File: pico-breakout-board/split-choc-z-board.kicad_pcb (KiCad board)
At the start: 2 copper layers, 147.1 x 106.5 mm, 79 parts, among them J1 USB4105-GF-A, J2 USB4105-GF-A, J3 Conn_01x04_Pin, J4 Conn_01x02, SW1 SW_SPST, SW10 SW_SPST, SW11 SW_SPST, SW12 SW_SPST, SW13 SW_SPST, SW14 SW_SPST, SW15 SW_SPST, SW16 SW_SPST, SW17 SW_SPST, SW18 SW_SPST, SW19 SW_SPST, SW2 SW_SPST, SW20 SW_SPST, SW21 SW_SPST, SW22 SW_SPST, SW3 SW_SPST, SW4 SW_SPST, SW5 SW_SPST, SW6 SW_SPST, SW7 SW_SPST, SW8 SW_SPST, SW9 SW_SPST, U2 RP2040, U3 NCP1117-3.3_SOT223, U4 W25Q128JVS, U5 USBLC6-2SC6, X1 ABM8-272-T3

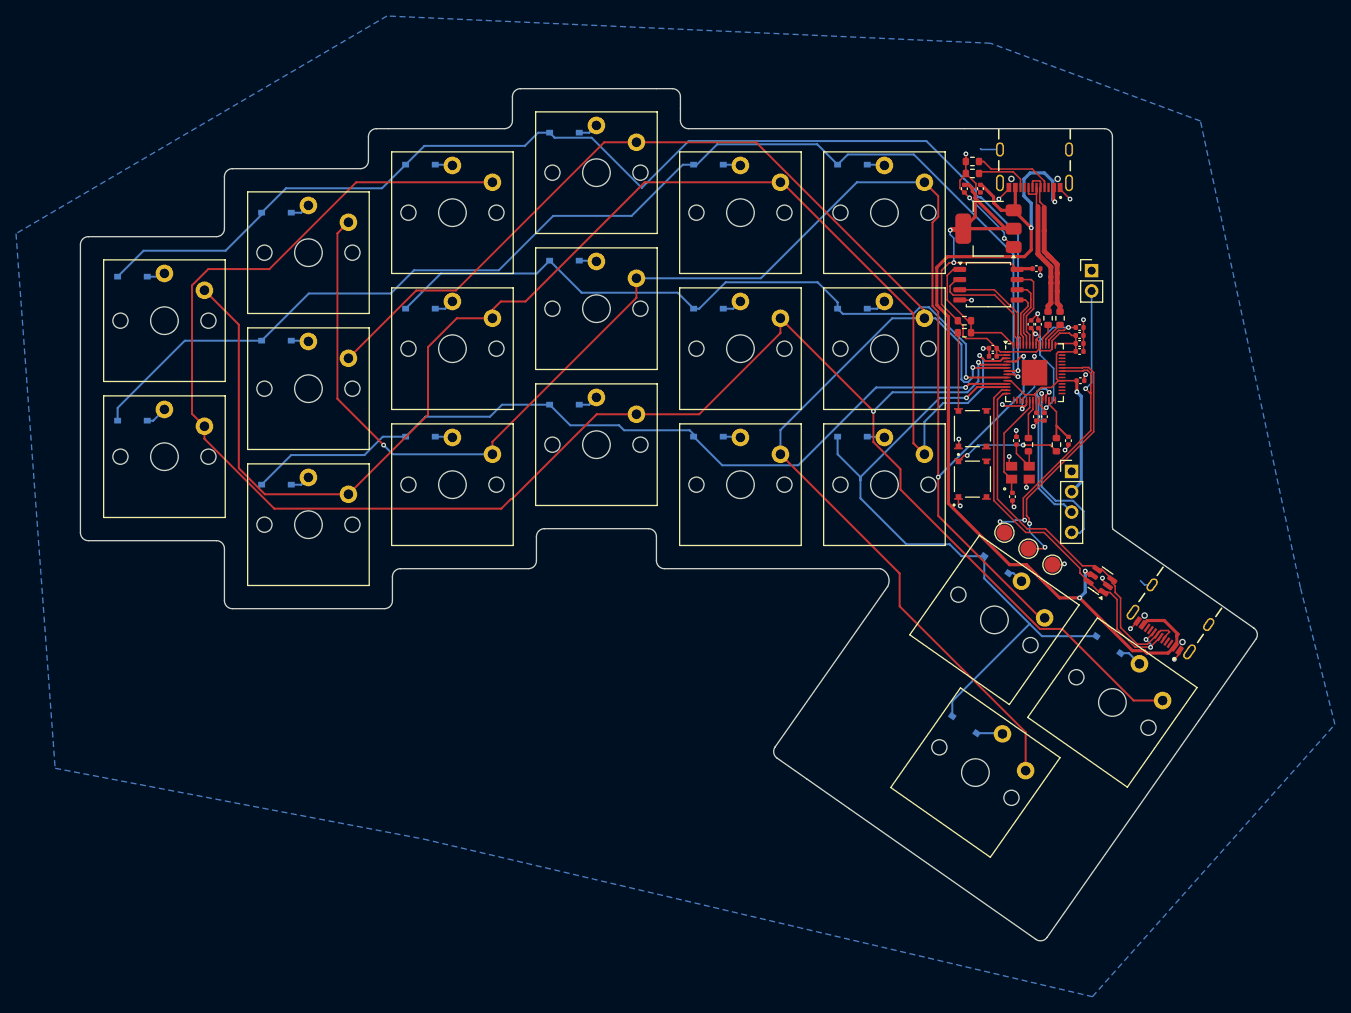
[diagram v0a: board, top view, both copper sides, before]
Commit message: Removed matrix and added 2.54mm pins 2x20
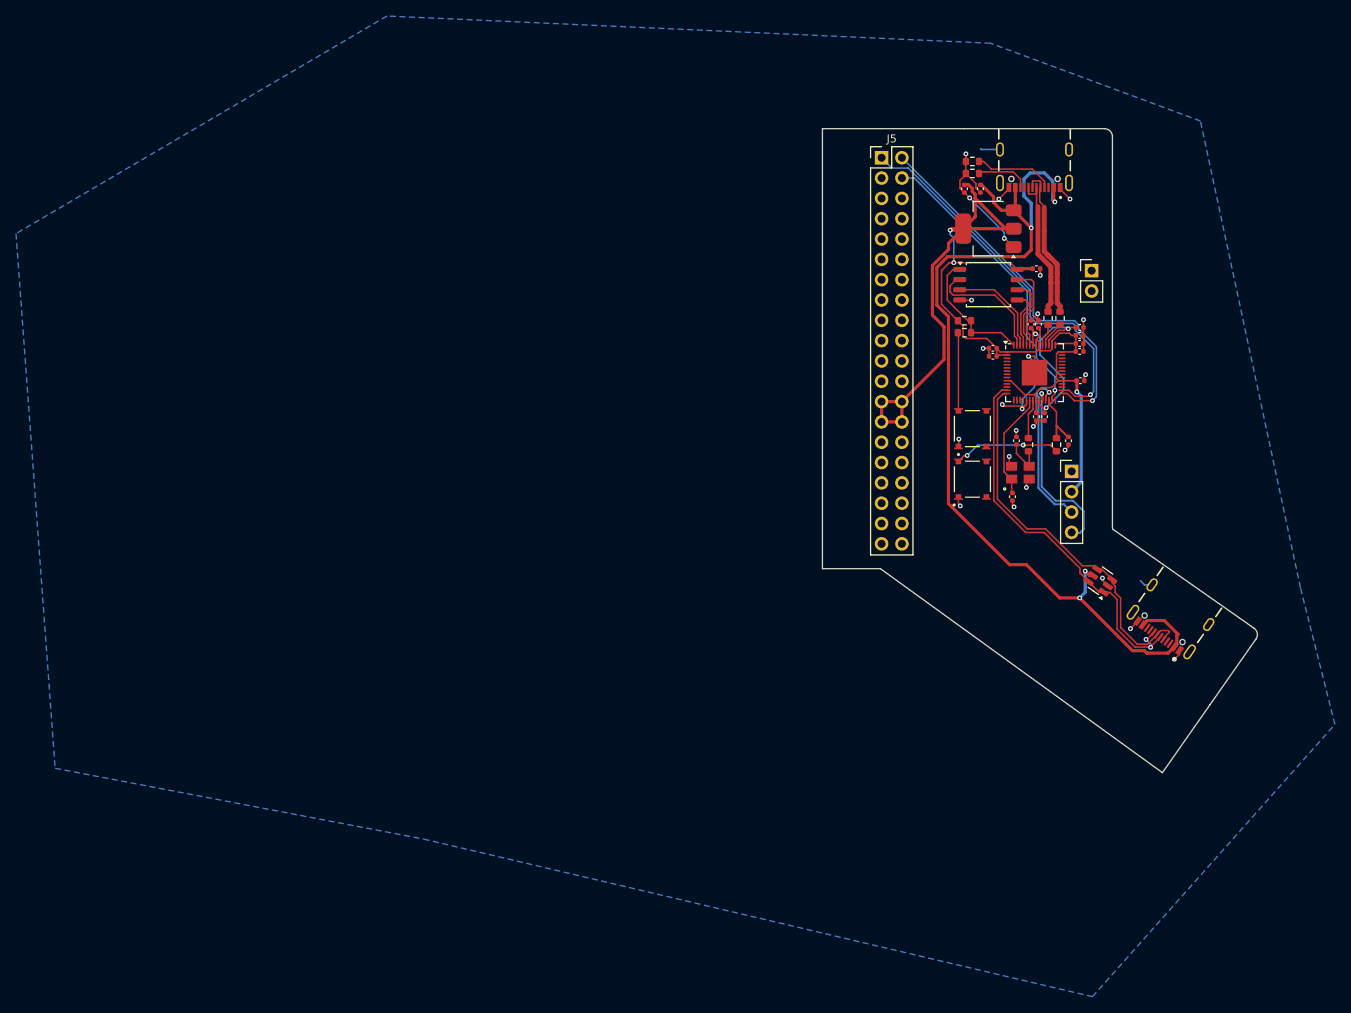
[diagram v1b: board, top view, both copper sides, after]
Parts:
- removed D1, D10, D11, D12, D13, D14, D15, D16, D17, D18, D19, D2, D20, D3, D4, D5, D6, D7, D8, D9: D, footprints:SOD123_MCC
- removed GND1, GP24, GP25: TestPoint, TestPoint:TestPoint_Pad_D2.0mm
- removed SW1, SW10, SW11, SW12, SW13, SW14, SW15, SW16, SW17, SW18, SW19, SW2, SW20, SW3, SW4, SW5, SW6, SW7, SW8, SW9: SW_SPST, ScottoKeebs_Choc:Choc_V1_1.00u
- added J5: Conn_02x20_Counter_Clockwise, Connector_PinHeader_2.54mm:PinHeader_2x20_P2.54mm_Vertical, F.Cu at (125.6, 49.1)
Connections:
- U2 pad 11: /Row_4 -> /GPIO8
- U2 pad 12: /Row_5 -> /GPIO9
- U2 pad 13: /B-B_D+ -> /GPIO10
- U2 pad 14: /B-B_D- -> /GPIO11
- U2 pad 15: unconnected-(U2-GPIO12-Pad15) -> /GPIO12
- U2 pad 16: unconnected-(U2-GPIO13-Pad16) -> /GPIO13
- U2 pad 17: unconnected-(U2-GPIO14-Pad17) -> /GPIO14
- U2 pad 18: unconnected-(U2-GPIO15-Pad18) -> /GPIO15
- U2 pad 2: +3V3 -> /GPIO0
- U2 pad 27: unconnected-(U2-GPIO16-Pad27) -> /GPIO16
- U2 pad 28: unconnected-(U2-GPIO17-Pad28) -> /GPIO17
- U2 pad 29: unconnected-(U2-GPIO18-Pad29) -> /GPIO18
- U2 pad 3: /Col_1 -> /GPIO1
- U2 pad 30: unconnected-(U2-GPIO19-Pad30) -> /GPIO19
- U2 pad 31: unconnected-(U2-GPIO20-Pad31) -> /GPIO20
- U2 pad 32: unconnected-(U2-GPIO21-Pad32) -> /GPIO21
- U2 pad 34: unconnected-(U2-GPIO22-Pad34) -> /GPIO22
- U2 pad 35: unconnected-(U2-GPIO23-Pad35) -> /GPIO23
- U2 pad 36: /GP24 -> /GPIO24
- U2 pad 37: /GP25 -> /GPIO25
- U2 pad 38: unconnected-(U2-GPIO26_ADC0-Pad38) -> /GPIO26
- U2 pad 39: unconnected-(U2-GPIO27_ADC1-Pad39) -> /GPIO27
- U2 pad 4: /Col_2 -> /GPIO2
- U2 pad 40: unconnected-(U2-GPIO28_ADC2-Pad40) -> /GPIO28
- U2 pad 41: unconnected-(U2-GPIO29_ADC3-Pad41) -> /GPIO29
- U2 pad 5: /Col_3 -> /GPIO3
- U2 pad 6: /Col_4 -> /GPIO4
- U2 pad 7: /Row_1 -> /GPIO5
- U2 pad 8: /Row_2 -> /GPIO6
- U2 pad 9: /Row_3 -> /GPIO7
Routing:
- net /Col_3: track 241.3 -> 0.00 mm, vias 2 -> 0
- net /Col_2: track 198.8 -> 0.00 mm, vias 3 -> 0
- net /Col_4: track 189.6 -> 0.00 mm, vias 1 -> 0
- net /Col_1: track 177.6 -> 0.00 mm, vias 1 -> 0
- net /Row_2: track 151.1 -> 0.00 mm, vias 1 -> 0
- net /Row_1: track 149.1 -> 0.00 mm, vias 1 -> 0
- net /Row_4: track 104.9 -> 0.00 mm, vias 1 -> 0
- net /Row_3: track 90.0 -> 0.00 mm, vias 1 -> 0
- net /Row_5: track 86.1 -> 0.00 mm, vias 1 -> 0
- net /GPIO19: track 0.00 -> 48.6 mm, vias 0 -> 1
- net /GPIO18: track 0.00 -> 47.5 mm, vias 0 -> 1
- net /GP24: track 43.9 -> 0.00 mm, vias 3 -> 0
- net /GPIO16: track 0.00 -> 36.8 mm, vias 0 -> 1
- net +3V3: track 109.6 -> 145.7 mm
- net /GP25: track 32.7 -> 0.00 mm, vias 2 -> 0
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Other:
- board size 147.1 x 106.5 mm -> 54.4 x 80.5 mm

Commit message: Finished bare redesign
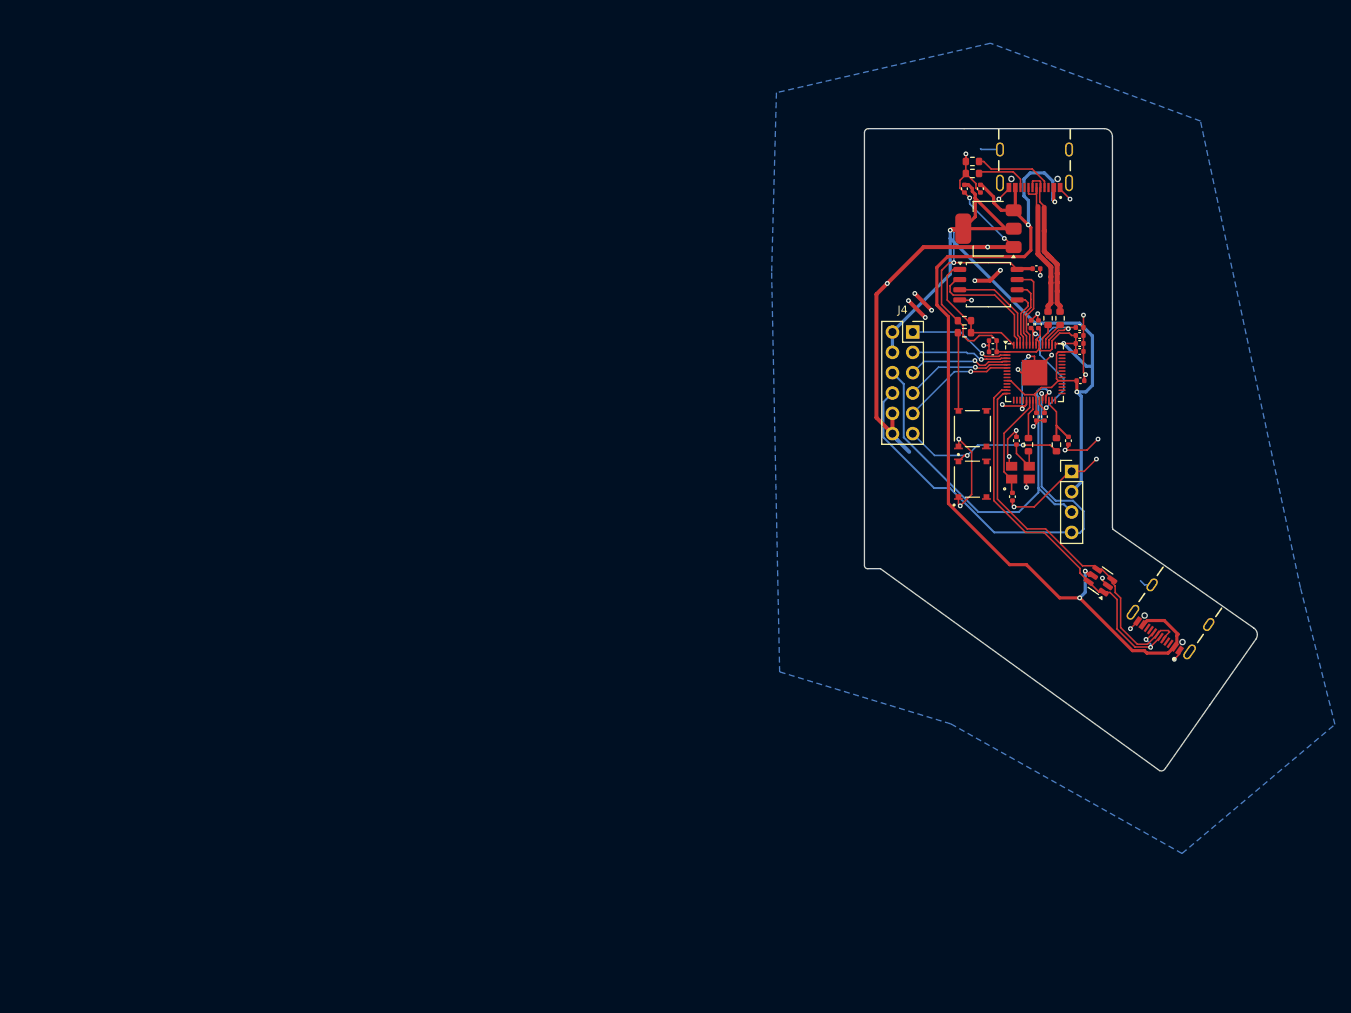
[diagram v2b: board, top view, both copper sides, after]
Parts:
- removed J5: Conn_02x20_Counter_Clockwise, Connector_PinHeader_2.54mm:PinHeader_2x20_P2.54mm_Vertical
- J4: value Conn_01x02 -> Conn_02x06_Odd_Even; footprint Connector_PinHeader_2.54mm:PinHeader_1x02_P2.54mm_Vertical -> Connector_PinSocket_2.54mm:PinSocket_2x06_P2.54mm_Vertical
- moved J4 23.6 mm to (129.5, 70.9)
- moved C8 0.95 mm to (139.6, 72.0)
- moved C7 0.55 mm to (139.6, 73.4)
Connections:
- J4 pad 1: GND -> /GPIO0
- J4 pad 2: /GP24 -> +3V3
- R8 pad 1: Net-(SW22-B) -> /RESET
- SW22 pad 2: Net-(SW22-B) -> /RESET
- U2 pad 11: /GPIO8 -> unconnected-(U2-GPIO8-Pad11)
- U2 pad 12: /GPIO9 -> unconnected-(U2-GPIO9-Pad12)
- U2 pad 13: /GPIO10 -> /B-B_D+
- U2 pad 14: /GPIO11 -> /B-B_D-
- U2 pad 15: /GPIO12 -> unconnected-(U2-GPIO12-Pad15)
- U2 pad 16: /GPIO13 -> unconnected-(U2-GPIO13-Pad16)
- U2 pad 17: /GPIO14 -> unconnected-(U2-GPIO14-Pad17)
- U2 pad 18: /GPIO15 -> unconnected-(U2-GPIO15-Pad18)
- U2 pad 27: /GPIO16 -> unconnected-(U2-GPIO16-Pad27)
- U2 pad 28: /GPIO17 -> unconnected-(U2-GPIO17-Pad28)
- U2 pad 29: /GPIO18 -> unconnected-(U2-GPIO18-Pad29)
- U2 pad 30: /GPIO19 -> unconnected-(U2-GPIO19-Pad30)
- U2 pad 31: /GPIO20 -> unconnected-(U2-GPIO20-Pad31)
- U2 pad 32: /GPIO21 -> unconnected-(U2-GPIO21-Pad32)
- U2 pad 34: /GPIO22 -> unconnected-(U2-GPIO22-Pad34)
- U2 pad 35: /GPIO23 -> unconnected-(U2-GPIO23-Pad35)
- U2 pad 36: /GPIO24 -> unconnected-(U2-GPIO24-Pad36)
- U2 pad 37: /GPIO25 -> unconnected-(U2-GPIO25-Pad37)
- U2 pad 38: /GPIO26 -> unconnected-(U2-GPIO26_ADC0-Pad38)
- U2 pad 39: /GPIO27 -> unconnected-(U2-GPIO27_ADC1-Pad39)
- U2 pad 40: /GPIO28 -> unconnected-(U2-GPIO28_ADC2-Pad40)
- U2 pad 41: /GPIO29 -> unconnected-(U2-GPIO29_ADC3-Pad41)
- U2 pad 7: /GPIO5 -> unconnected-(U2-GPIO5-Pad7)
- U2 pad 8: /GPIO6 -> unconnected-(U2-GPIO6-Pad8)
- U2 pad 9: /GPIO7 -> unconnected-(U2-GPIO7-Pad9)
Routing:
- net GND: track 64.7 -> 157.4 mm, vias 25 -> 37
- net /GPIO19: track 48.6 -> 0.00 mm, vias 1 -> 0
- net /GPIO18: track 47.5 -> 0.00 mm, vias 1 -> 0
- net /GPIO16: track 36.8 -> 0.00 mm, vias 1 -> 0
- net /DEBUG_CLK: track 23.0 -> 57.5 mm
- net /DEBUG_DATA: track 20.5 -> 51.5 mm
- net /RESET: track 0.00 -> 21.4 mm, vias 0 -> 2
- net +3V3: track 145.7 -> 163.2 mm, vias 3 -> 4
- net /GPIO4: track 0.00 -> 14.1 mm, vias 0 -> 1
- net Net-(SW22-B): track 13.4 -> 0.00 mm, vias 2 -> 0
- net /GPIO3: track 0.00 -> 13.3 mm, vias 0 -> 1
- net /GPIO0: track 0.00 -> 13.3 mm, vias 0 -> 1
- net /GPIO2: track 0.00 -> 12.8 mm, vias 0 -> 1
- net /GPIO1: track 0.00 -> 12.2 mm, vias 0 -> 1
- net VBUS: track 121.4 -> 120.5 mm
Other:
- board size 54.4 x 80.5 mm -> 49.1 x 80.3 mm
- board text added: "Zain Kergaye 9/24/25"
- board text removed: "Zain Kergaye 6/24/25"

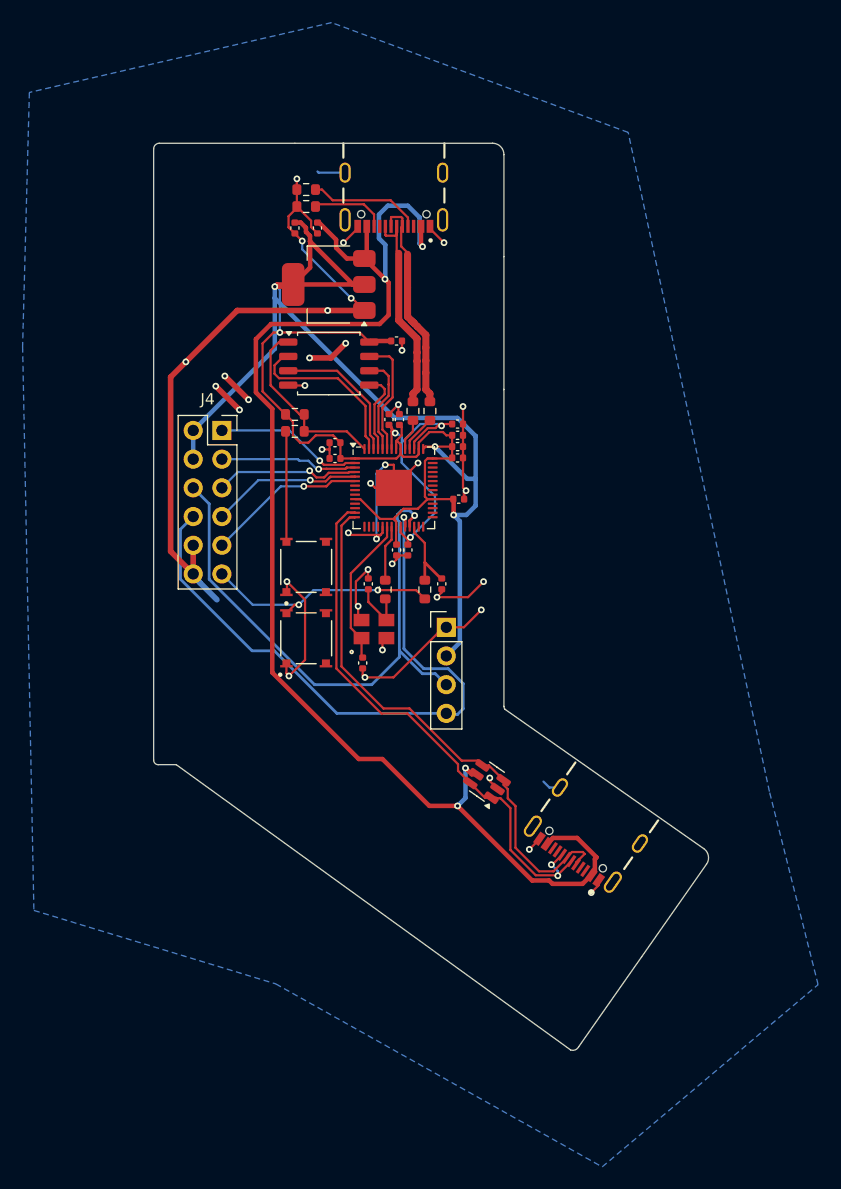
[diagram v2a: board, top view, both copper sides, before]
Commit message: Completed first design review redesign
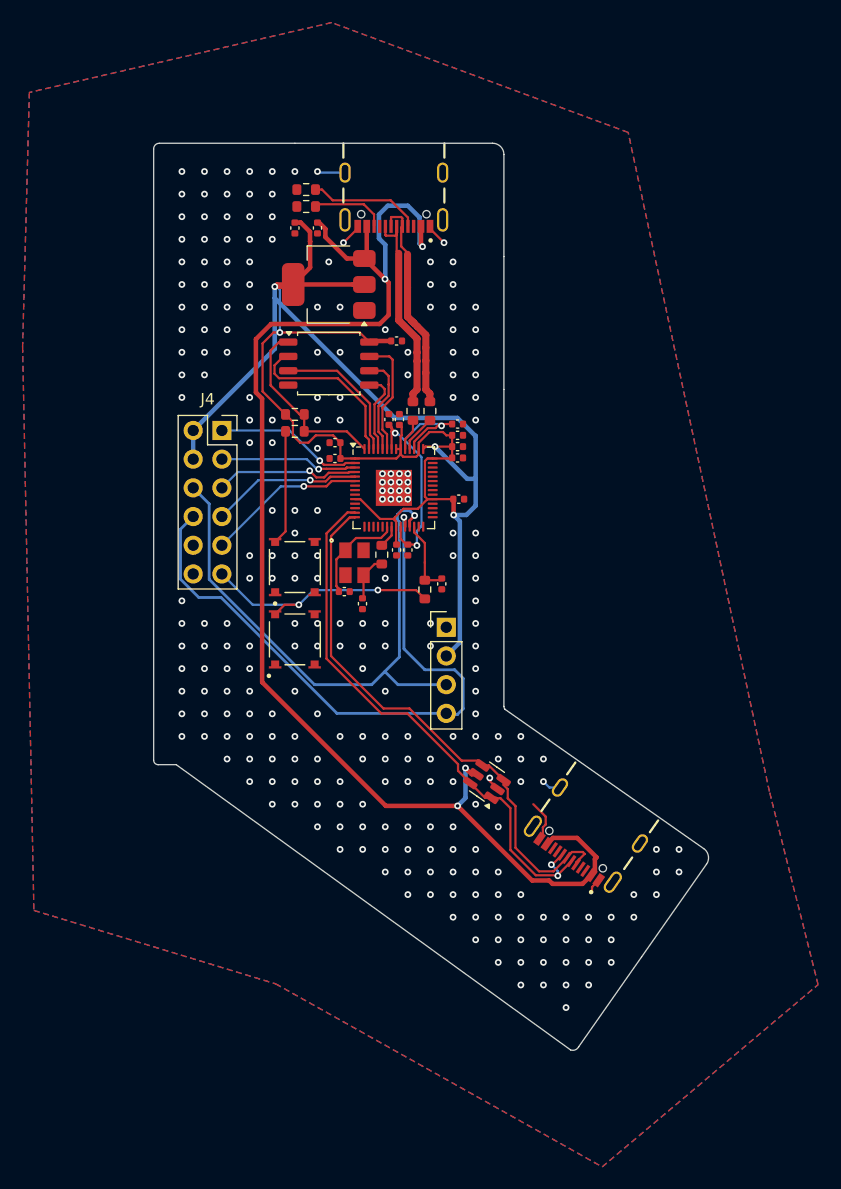
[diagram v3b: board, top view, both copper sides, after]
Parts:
- moved C15 6.52 mm to (140.4, 85.2), turned to 180 degrees
- moved X1 6.12 mm to (141.3, 82.6), turned to 0 degrees
- moved R7 3.10 mm to (143.7, 81.9)
- moved C16 1.83 mm to (142.0, 86.3), turned to -90 degrees
- moved SW22 1.00 mm to (136.0, 89.4)
- moved SW21 1.00 mm to (136.0, 83.0)
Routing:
- net GND: track 157.4 -> 14.6 mm, vias 37 -> 260
- net +3V3: track 163.2 -> 157.2 mm
- net /XIN: track 13.4 -> 8.99 mm
- net /XOUT: track 4.97 -> 2.01 mm
- net +1V1: track 27.9 -> 25.8 mm
- net Net-(C16-Pad1): track 5.30 -> 4.11 mm
- net /RESET: track 21.4 -> 22.4 mm
- net VBUS: track 120.5 -> 121.6 mm
- net /B-B_D-: track 47.8 -> 48.6 mm
- net /B-B_D+: track 48.9 -> 49.6 mm
- net /DEBUG_DATA: track 51.5 -> 52.0 mm
- added copper zone on F.Cu, net GND
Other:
- board text added: "Zain Kergaye 10/4/25"
- board text removed: "Zain Kergaye 9/24/25"

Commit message: Completed second design review redesign
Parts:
- turned C12 to 90 degrees
- turned C13 to 90 degrees
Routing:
- net +3V3: track 157.2 -> 149.4 mm
- net VBUS: track 121.6 -> 120.7 mm
- net GND: track 14.6 -> 13.9 mm, vias 260 -> 259
